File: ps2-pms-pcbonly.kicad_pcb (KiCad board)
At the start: 2 copper layers, 54.7 x 47 mm, 97 parts, among them U1 ADP151, U2 SC174, U3 TPS61253, U4 BQ24076, U5 CSD22202W15

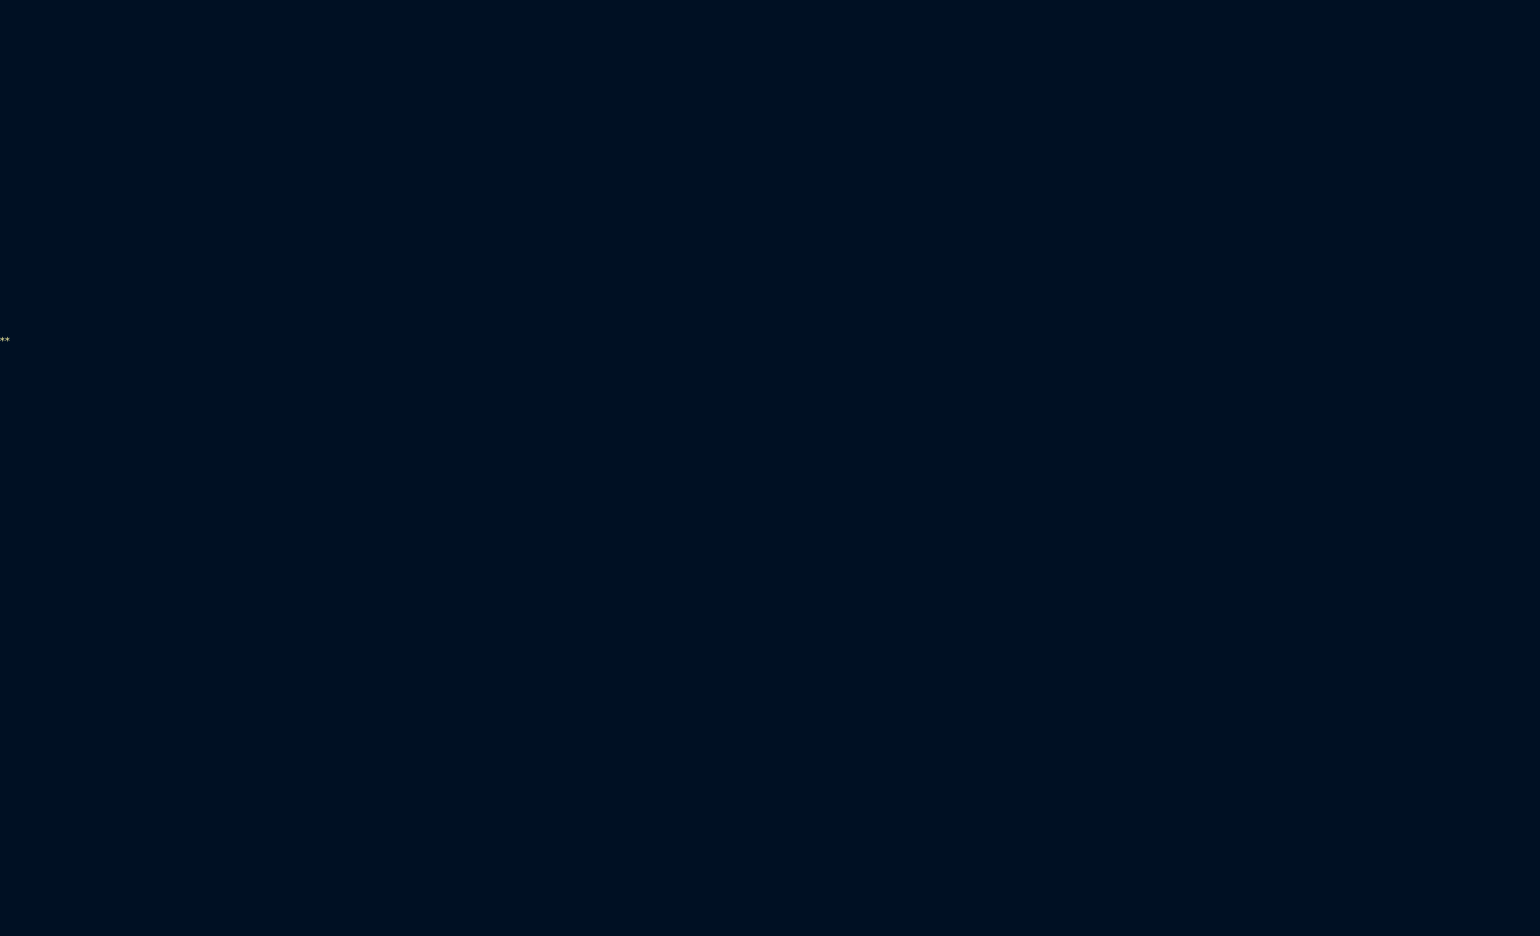
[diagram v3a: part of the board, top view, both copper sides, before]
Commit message: build(ps2-pms): New version with less dead space, shrunk PCB down by 2x1cm
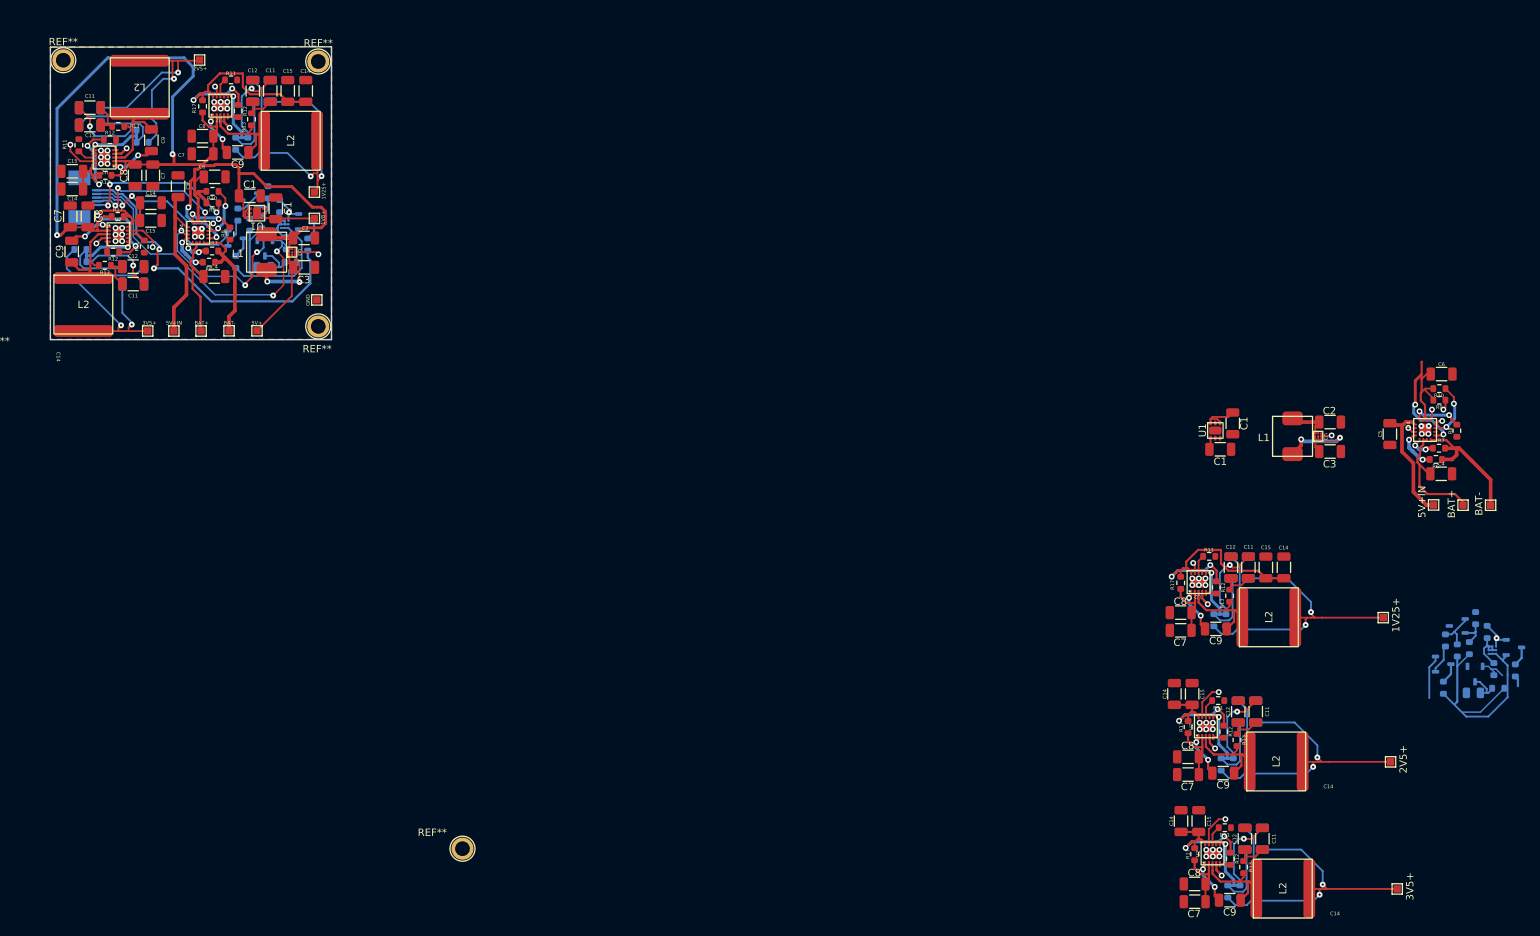
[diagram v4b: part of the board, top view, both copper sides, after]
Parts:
- added 1V25+: TestPoint_Pad_1.0x1.0mm, TestPoint:TestPoint_Pad_1.0x1.0mm, F.Cu at (261.5, 92.8)
- added 1V25+: TestPoint_Pad_1.0x1.0mm, TestPoint:TestPoint_Pad_1.0x1.0mm, F.Cu at (116.3, 35.0)
- added 1V8+: TestPoint_Pad_1.0x1.0mm, TestPoint:TestPoint_Pad_1.0x1.0mm, F.Cu at (116.3, 38.5)
- added 2V5+: TestPoint_Pad_1.0x1.0mm, TestPoint:TestPoint_Pad_1.0x1.0mm, F.Cu at (100.7, 17.0)
- added 2V5+: TestPoint_Pad_1.0x1.0mm, TestPoint:TestPoint_Pad_1.0x1.0mm, F.Cu at (262.5, 112.4)
- added 3V5+: TestPoint_Pad_1.0x1.0mm, TestPoint:TestPoint_Pad_1.0x1.0mm, F.Cu at (93.6, 53.9)
- added 3V5+: TestPoint_Pad_1.0x1.0mm, TestPoint:TestPoint_Pad_1.0x1.0mm, F.Cu at (263.4, 129.7)
- added 5-pin: 5pin FPC, ps2+:5pin FPC, B.Cu at (83.3, 35.7)
- added 5V+: TestPoint_Pad_1.0x1.0mm, TestPoint:TestPoint_Pad_1.0x1.0mm, F.Cu at (108.5, 53.8)
- added 5V+IN: TestPoint_Pad_1.0x1.0mm, TestPoint:TestPoint_Pad_1.0x1.0mm, F.Cu at (97.2, 53.9)
- added 5V+IN: TestPoint_Pad_1.0x1.0mm, TestPoint:TestPoint_Pad_1.0x1.0mm, F.Cu at (268.4, 77.5)
- added BAT+: TestPoint_Pad_1.0x1.0mm, TestPoint:TestPoint_Pad_1.0x1.0mm, F.Cu at (272.4, 77.5)
- added BAT+: TestPoint_Pad_1.0x1.0mm, TestPoint:TestPoint_Pad_1.0x1.0mm, F.Cu at (100.9, 53.9)
- added BAT-: TestPoint_Pad_1.0x1.0mm, TestPoint:TestPoint_Pad_1.0x1.0mm, F.Cu at (104.7, 53.8)
- added BAT-: TestPoint_Pad_1.0x1.0mm, TestPoint:TestPoint_Pad_1.0x1.0mm, F.Cu at (276.1, 77.5)
- added BC846: BC846A, ps2-pms:BC846A, B.Cu at (274.0, 100.5)
- added BC846: BC846A, ps2-pms:BC846A, B.Cu at (279.3, 96.8)
- added BC846: BC846A, ps2-pms:BC846A, B.Cu at (109.5, 42.6)
- added BC846: BC846A, ps2-pms:BC846A, B.Cu at (115.2, 39.0)
- added BC847C: BC846A, ps2-pms:BC846A, B.Cu at (269.7, 99.1)
- added BC847C: BC846A, ps2-pms:BC846A, B.Cu at (105.6, 41.2)
- added C1: C_1206_3216Metric, Capacitor_SMD:C_1206_3216Metric, F.Cu at (239.4, 69.9)
- added C1: 1uF, Capacitor_SMD:C_1206_3216Metric, F.Cu at (107.5, 35.5)
- added C1: C_1206_3216Metric, Capacitor_SMD:C_1206_3216Metric, F.Cu at (111.0, 37.2)
- added C1: 1uF, Capacitor_SMD:C_1206_3216Metric, F.Cu at (241.1, 66.4)
- added C10: C_1206_3216Metric, Capacitor_SMD:C_1206_3216Metric, B.Cu at (107.9, 21.2)
- added C10: C_1206_3216Metric, Capacitor_SMD:C_1206_3216Metric, B.Cu at (240.8, 86.0)
- added C10: C_1206_3216Metric, Capacitor_SMD:C_1206_3216Metric, B.Cu at (91.7, 45.1)
- added C10: C_1206_3216Metric, Capacitor_SMD:C_1206_3216Metric, B.Cu at (85.8, 25.9)
- added C10: C_1206_3216Metric, Capacitor_SMD:C_1206_3216Metric, B.Cu at (241.8, 105.6)
- added C10: C_1206_3216Metric, Capacitor_SMD:C_1206_3216Metric, B.Cu at (242.7, 122.8)
- added C11: C_1206_3216Metric, Capacitor_SMD:C_1206_3216Metric, F.Cu at (85.8, 23.5)
- added C11: C_1206_3216Metric, Capacitor_SMD:C_1206_3216Metric, F.Cu at (243.2, 86.0)
- added C11: C_1206_3216Metric, Capacitor_SMD:C_1206_3216Metric, F.Cu at (245.1, 122.8)
- added C11: C_1206_3216Metric, Capacitor_SMD:C_1206_3216Metric, F.Cu at (110.3, 21.2)
- added C11: C_1206_3216Metric, Capacitor_SMD:C_1206_3216Metric, F.Cu at (91.7, 47.5)
- added C11: C_1206_3216Metric, Capacitor_SMD:C_1206_3216Metric, F.Cu at (244.2, 105.6)
- added C12: C_1206_3216Metric, Capacitor_SMD:C_1206_3216Metric, F.Cu at (240.8, 86.0)
- added C12: C_1206_3216Metric, Capacitor_SMD:C_1206_3216Metric, F.Cu at (241.8, 105.6)
- added C12: C_1206_3216Metric, Capacitor_SMD:C_1206_3216Metric, F.Cu at (91.7, 45.1)
- added C12: C_1206_3216Metric, Capacitor_SMD:C_1206_3216Metric, F.Cu at (242.7, 122.8)
- added C12: C_1206_3216Metric, Capacitor_SMD:C_1206_3216Metric, F.Cu at (85.8, 25.9)
- added C12: C_1206_3216Metric, Capacitor_SMD:C_1206_3216Metric, F.Cu at (107.9, 21.2)
- added C13: C_1206_3216Metric, Capacitor_SMD:C_1206_3216Metric, B.Cu at (91.7, 47.5)
- added C13: C_1206_3216Metric, Capacitor_SMD:C_1206_3216Metric, B.Cu at (110.3, 21.2)
- added C13: C_1206_3216Metric, Capacitor_SMD:C_1206_3216Metric, B.Cu at (85.8, 23.5)
- added C13: C_1206_3216Metric, Capacitor_SMD:C_1206_3216Metric, B.Cu at (245.1, 122.8)
- added C13: C_1206_3216Metric, Capacitor_SMD:C_1206_3216Metric, B.Cu at (243.2, 86.0)
- added C13: C_1206_3216Metric, Capacitor_SMD:C_1206_3216Metric, B.Cu at (244.2, 105.6)
- added C14: C_1206_3216Metric, Capacitor_SMD:C_1206_3216Metric, F.Cu at (115.1, 21.2)
- added C14: C_1206_3216Metric, Capacitor_SMD:C_1206_3216Metric, F.Cu at (94.0, 36.4)
- added C14: C_1206_3216Metric, Capacitor_SMD:C_1206_3216Metric, F.Cu at (248.0, 86.0)
- added C14: C_1206_3216Metric, Capacitor_SMD:C_1206_3216Metric, F.Cu at (234.0, 120.4)
- added C14: C_1206_3216Metric, Capacitor_SMD:C_1206_3216Metric, F.Cu at (233.1, 103.2)
- added C14: C_1206_3216Metric, Capacitor_SMD:C_1206_3216Metric, F.Cu at (83.4, 34.6)
- added C15: C_1206_3216Metric, Capacitor_SMD:C_1206_3216Metric, F.Cu at (235.6, 103.2)
- added C15: C_1206_3216Metric, Capacitor_SMD:C_1206_3216Metric, F.Cu at (236.5, 120.4)
- added C15: C_1206_3216Metric, Capacitor_SMD:C_1206_3216Metric, F.Cu at (112.7, 21.2)
- added C15: C_1206_3216Metric, Capacitor_SMD:C_1206_3216Metric, F.Cu at (94.0, 38.8)
- added C15: C_1206_3216Metric, Capacitor_SMD:C_1206_3216Metric, F.Cu at (83.4, 32.1)
- added C15: C_1206_3216Metric, Capacitor_SMD:C_1206_3216Metric, F.Cu at (245.6, 86.0)
- added C16: C_0805_2012Metric, Capacitor_SMD:C_0805_2012Metric, B.Cu at (109.4, 45.2)
- added C16: C_0805_2012Metric, Capacitor_SMD:C_0805_2012Metric, B.Cu at (273.8, 103.0)
- added C2: C_1206_3216Metric, Capacitor_SMD:C_1206_3216Metric, F.Cu at (254.3, 66.2)
- added C2: C_1206_3216Metric, Capacitor_SMD:C_1206_3216Metric, F.Cu at (114.9, 41.2)
- added C3: C_1206_3216Metric, Capacitor_SMD:C_1206_3216Metric, F.Cu at (114.9, 45.2)
- added C3: C_1206_3216Metric, Capacitor_SMD:C_1206_3216Metric, F.Cu at (254.3, 70.2)
- added C4: C_1206_3216Metric, Capacitor_SMD:C_1206_3216Metric, F.Cu at (102.7, 46.5)
- added C4: C_1206_3216Metric, Capacitor_SMD:C_1206_3216Metric, F.Cu at (269.4, 73.3)
- added C5: C_1206_3216Metric, Capacitor_SMD:C_1206_3216Metric, F.Cu at (97.8, 34.2)
- added C5: C_1206_3216Metric, Capacitor_SMD:C_1206_3216Metric, F.Cu at (262.4, 67.9)
- added C6: C_1206_3216Metric, Capacitor_SMD:C_1206_3216Metric, F.Cu at (102.7, 32.9)
- added C6: C_1206_3216Metric, Capacitor_SMD:C_1206_3216Metric, F.Cu at (269.5, 59.7)
- added C7: C_1206_3216Metric, Capacitor_SMD:C_1206_3216Metric, F.Cu at (235.9, 131.4)
- added C7: C_1206_3216Metric, Capacitor_SMD:C_1206_3216Metric, F.Cu at (234.0, 94.5)
- added C7: C_1206_3216Metric, Capacitor_SMD:C_1206_3216Metric, F.Cu at (101.1, 29.8)
- added C7: C_1206_3216Metric, Capacitor_SMD:C_1206_3216Metric, F.Cu at (83.1, 38.3)
- added C7: C_1206_3216Metric, Capacitor_SMD:C_1206_3216Metric, F.Cu at (94.3, 32.7)
- added C7: C_1206_3216Metric, Capacitor_SMD:C_1206_3216Metric, F.Cu at (235.0, 114.1)
- added C8: C_1206_3216Metric, Capacitor_SMD:C_1206_3216Metric, F.Cu at (235.0, 111.7)
- added C8: C_1206_3216Metric, Capacitor_SMD:C_1206_3216Metric, F.Cu at (234.0, 92.1)
- added C8: C_1206_3216Metric, Capacitor_SMD:C_1206_3216Metric, F.Cu at (101.1, 27.4)
- added C8: C_1206_3216Metric, Capacitor_SMD:C_1206_3216Metric, F.Cu at (235.9, 129.0)
- added C8: C_1206_3216Metric, Capacitor_SMD:C_1206_3216Metric, F.Cu at (91.9, 32.7)
- added C8: C_1206_3216Metric, Capacitor_SMD:C_1206_3216Metric, F.Cu at (85.5, 38.3)
- added C9: C_1206_3216Metric, Capacitor_SMD:C_1206_3216Metric, F.Cu at (83.3, 43.1)
- added C9: C_1206_3216Metric, Capacitor_SMD:C_1206_3216Metric, F.Cu at (238.8, 94.3)
- added C9: C_1206_3216Metric, Capacitor_SMD:C_1206_3216Metric, F.Cu at (240.7, 131.2)
- added C9: C_1206_3216Metric, Capacitor_SMD:C_1206_3216Metric, F.Cu at (94.1, 27.9)
- added C9: C_1206_3216Metric, Capacitor_SMD:C_1206_3216Metric, F.Cu at (239.8, 113.9)
- added C9: C_1206_3216Metric, Capacitor_SMD:C_1206_3216Metric, F.Cu at (105.9, 29.6)
- added G***: LOGO, graphics:iblis 5mm, B.Cu at (90.3, 38.2)
- added GND: TestPoint_Pad_1.0x1.0mm, TestPoint:TestPoint_Pad_1.0x1.0mm, F.Cu at (116.6, 49.6)
- added L1: Inductor-1uH, ps2-pms:Inductor-1uH, F.Cu at (109.8, 43.1)
- added L1: Inductor-1uH, ps2-pms:Inductor-1uH, F.Cu at (249.2, 68.2)
- added L2: inductor-2uh, ps2-pms:inductor-2uh, F.Cu at (113.0, 28.0)
- added L2: inductor-2uh, ps2-pms:inductor-2uh, F.Cu at (92.5, 20.7)
- added L2: inductor-2uh, ps2-pms:inductor-2uh, F.Cu at (247.9, 129.6)
- added L2: inductor-2uh, ps2-pms:inductor-2uh, F.Cu at (246.0, 92.8)
- added L2: inductor-2uh, ps2-pms:inductor-2uh, F.Cu at (84.9, 50.2)
- added L2: inductor-2uh, ps2-pms:inductor-2uh, F.Cu at (247.0, 112.3)
- added R1: R_0603_1608Metric, Resistor_SMD:R_0603_1608Metric, B.Cu at (110.0, 35.0)
- added R1: R_0603_1608Metric, Resistor_SMD:R_0603_1608Metric, B.Cu at (274.1, 92.9)
- added R10: R_0603_1608Metric, Resistor_SMD:R_0603_1608Metric, F.Cu at (102.4, 34.9)
- added R10: R_0603_1608Metric, Resistor_SMD:R_0603_1608Metric, F.Cu at (269.2, 61.7)
- added R11: R_0603_1608Metric, Resistor_SMD:R_0603_1608Metric, F.Cu at (239.1, 104.1)
- added R11: R_0603_1608Metric, Resistor_SMD:R_0603_1608Metric, F.Cu at (105.0, 19.7)
- added R11: R_0603_1608Metric, Resistor_SMD:R_0603_1608Metric, F.Cu at (237.9, 84.5)
- added R11: R_0603_1608Metric, Resistor_SMD:R_0603_1608Metric, F.Cu at (84.3, 28.6)
- added R11: R_0603_1608Metric, Resistor_SMD:R_0603_1608Metric, F.Cu at (240.0, 121.3)
- added R11: R_0603_1608Metric, Resistor_SMD:R_0603_1608Metric, F.Cu at (93.2, 42.4)
- added R12: R_0603_1608Metric, Resistor_SMD:R_0603_1608Metric, F.Cu at (239.8, 108.3)
- added R12: R_0603_1608Metric, Resistor_SMD:R_0603_1608Metric, F.Cu at (105.9, 23.9)
- added R12: R_0603_1608Metric, Resistor_SMD:R_0603_1608Metric, F.Cu at (88.9, 43.1)
- added R12: R_0603_1608Metric, Resistor_SMD:R_0603_1608Metric, F.Cu at (238.8, 88.7)
- added R12: R_0603_1608Metric, Resistor_SMD:R_0603_1608Metric, F.Cu at (240.8, 125.6)
- added R12: R_0603_1608Metric, Resistor_SMD:R_0603_1608Metric, F.Cu at (88.5, 27.9)
- added R13: R_0603_1608Metric, Resistor_SMD:R_0603_1608Metric, F.Cu at (242.6, 126.7)
- added R13: R_0603_1608Metric, Resistor_SMD:R_0603_1608Metric, F.Cu at (89.6, 26.1)
- added R13: R_0603_1608Metric, Resistor_SMD:R_0603_1608Metric, F.Cu at (240.7, 89.8)
- added R13: R_0603_1608Metric, Resistor_SMD:R_0603_1608Metric, F.Cu at (241.7, 109.4)
- added R13: R_0603_1608Metric, Resistor_SMD:R_0603_1608Metric, F.Cu at (107.7, 25.1)
- added R13: R_0603_1608Metric, Resistor_SMD:R_0603_1608Metric, F.Cu at (87.8, 44.9)
- added R14: R_0603_1608Metric, Resistor_SMD:R_0603_1608Metric, B.Cu at (105.6, 28.4)
- added R14: R_0603_1608Metric, Resistor_SMD:R_0603_1608Metric, B.Cu at (238.5, 93.2)
- added R15: R_0603_1608Metric, Resistor_SMD:R_0603_1608Metric, B.Cu at (240.2, 93.2)
- added R15: R_0603_1608Metric, Resistor_SMD:R_0603_1608Metric, B.Cu at (107.2, 28.4)
- added R15: R_0603_1608Metric, Resistor_SMD:R_0603_1608Metric, B.Cu at (241.2, 112.7)
- added R15: R_0603_1608Metric, Resistor_SMD:R_0603_1608Metric, B.Cu at (92.9, 26.6)
- added R15: R_0603_1608Metric, Resistor_SMD:R_0603_1608Metric, B.Cu at (84.5, 44.4)
- added R15: R_0603_1608Metric, Resistor_SMD:R_0603_1608Metric, B.Cu at (242.1, 130.0)
- added R17: R_0603_1608Metric, Resistor_SMD:R_0603_1608Metric, F.Cu at (101.1, 23.3)
- added R17: R_0603_1608Metric, Resistor_SMD:R_0603_1608Metric, B.Cu at (275.7, 94.7)
- added R17: R_0603_1608Metric, Resistor_SMD:R_0603_1608Metric, B.Cu at (111.5, 36.9)
- added R17: R_0603_1608Metric, Resistor_SMD:R_0603_1608Metric, F.Cu at (234.0, 88.1)
- added R17: R_0603_1608Metric, Resistor_SMD:R_0603_1608Metric, F.Cu at (235.9, 124.9)
- added R17: R_0603_1608Metric, Resistor_SMD:R_0603_1608Metric, F.Cu at (89.5, 38.3)
- added R17: R_0603_1608Metric, Resistor_SMD:R_0603_1608Metric, F.Cu at (87.9, 32.7)
- added R17: R_0603_1608Metric, Resistor_SMD:R_0603_1608Metric, F.Cu at (235.0, 107.7)
- added R18: R_0603_1608Metric, Resistor_SMD:R_0603_1608Metric, B.Cu at (279.5, 100.0)
- added R18: R_0603_1608Metric, Resistor_SMD:R_0603_1608Metric, B.Cu at (115.4, 42.1)
- added R19: R_0603_1608Metric, Resistor_SMD:R_0603_1608Metric, B.Cu at (276.6, 99.8)
- added R19: R_0603_1608Metric, Resistor_SMD:R_0603_1608Metric, B.Cu at (112.5, 41.9)
- added R2: R_0603_1608Metric, Resistor_SMD:R_0603_1608Metric, B.Cu at (109.1, 39.1)
- added R2: R_0603_1608Metric, Resistor_SMD:R_0603_1608Metric, B.Cu at (273.2, 96.9)
- added R20: R_0603_1608Metric, Resistor_SMD:R_0603_1608Metric, B.Cu at (113.0, 44.5)
- added R20: R_0603_1608Metric, Resistor_SMD:R_0603_1608Metric, B.Cu at (277.2, 102.4)
- added R21: R_0603_1608Metric, Resistor_SMD:R_0603_1608Metric, B.Cu at (239.5, 112.7)
- added R21: R_0603_1608Metric, Resistor_SMD:R_0603_1608Metric, B.Cu at (92.9, 28.2)
- added R22: R_0603_1608Metric, Resistor_SMD:R_0603_1608Metric, B.Cu at (240.4, 130.0)
- added R22: R_0603_1608Metric, Resistor_SMD:R_0603_1608Metric, B.Cu at (84.5, 42.8)
- added R3: R_0603_1608Metric, Resistor_SMD:R_0603_1608Metric, B.Cu at (270.0, 95.9)
- added R3: R_0603_1608Metric, Resistor_SMD:R_0603_1608Metric, B.Cu at (105.9, 38.0)
- added R4: R_0603_1608Metric, Resistor_SMD:R_0603_1608Metric, B.Cu at (107.5, 39.4)
- added R4: R_0603_1608Metric, Resistor_SMD:R_0603_1608Metric, B.Cu at (271.6, 97.3)
- added R5: R_0603_1608Metric, Resistor_SMD:R_0603_1608Metric, B.Cu at (269.7, 102.3)
- added R5: R_0603_1608Metric, Resistor_SMD:R_0603_1608Metric, B.Cu at (105.6, 44.5)
- added R6: R_0603_1608Metric, Resistor_SMD:R_0603_1608Metric, F.Cu at (268.7, 71.3)
- added R6: R_0603_1608Metric, Resistor_SMD:R_0603_1608Metric, F.Cu at (102.0, 44.5)
- added R7: R_0603_1608Metric, Resistor_SMD:R_0603_1608Metric, F.Cu at (269.1, 69.8)
- added R7: R_0603_1608Metric, Resistor_SMD:R_0603_1608Metric, F.Cu at (102.4, 43.0)
- added R8: R_0603_1608Metric, Resistor_SMD:R_0603_1608Metric, F.Cu at (104.8, 40.6)
- added R8: R_0603_1608Metric, Resistor_SMD:R_0603_1608Metric, F.Cu at (271.5, 67.4)
- added R9: R_0603_1608Metric, Resistor_SMD:R_0603_1608Metric, F.Cu at (269.2, 63.3)
- added R9: R_0603_1608Metric, Resistor_SMD:R_0603_1608Metric, F.Cu at (102.4, 36.5)
- added REF**: TestPoint_Plated_Hole_D2.0mm, TestPoint:TestPoint_Plated_Hole_D2.0mm, F.Cu at (116.8, 53.2)
- added REF**: TestPoint_Plated_Hole_D2.0mm, TestPoint:TestPoint_Plated_Hole_D2.0mm, F.Cu at (116.8, 17.2)
- added REF**: TestPoint_Plated_Hole_D2.0mm, TestPoint:TestPoint_Plated_Hole_D2.0mm, F.Cu at (82.2, 17.1)
- added REF**: TestPoint_Plated_Hole_D2.0mm, TestPoint:TestPoint_Plated_Hole_D2.0mm, F.Cu at (136.4, 124.2)
- added TL431: TL431, ps2-pms:TL431, B.Cu at (271.6, 93.9)
- added TL431: TL431, ps2-pms:TL431, B.Cu at (107.5, 36.1)
- added U1: ADP151, ps2-pms:ADP151, F.Cu at (238.7, 67.4)
- added U1: ADP151, ps2-pms:ADP151, F.Cu at (108.5, 37.8)
- added U2: SC174, ps2-pms:SC174, F.Cu at (238.3, 124.8)
- added U2: SC174, ps2-pms:SC174, F.Cu at (103.5, 23.2)
- added U2: SC174, ps2-pms:SC174, F.Cu at (236.4, 88.0)
- added U2: SC174, ps2-pms:SC174, F.Cu at (89.7, 40.7)
- added U2: SC174, ps2-pms:SC174, F.Cu at (87.8, 30.3)
- added U2: SC174, ps2-pms:SC174, F.Cu at (237.4, 107.6)
- added U3: TPS61253, ps2-pms:TPS61253, F.Cu at (252.7, 68.2)
- added U3: TPS61253, ps2-pms:TPS61253, F.Cu at (113.3, 43.1)
- added U4: BQ24076, ps2-pms:BQ24076, F.Cu at (100.5, 40.5)
- added U4: BQ24076, ps2-pms:BQ24076, F.Cu at (267.2, 67.3)
- added U5: CSD22202W15, ucb-c adapter:CSD22202W15, B.Cu at (112.2, 39.4)
- added U5: CSD22202W15, ucb-c adapter:CSD22202W15, B.Cu at (276.4, 97.2)
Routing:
- net 3V8+: track 154.7 -> 379.7 mm, vias 6 -> 12
- net FB: track 93.1 -> 260.4 mm, vias 6 -> 18
- net VDD: track 59.1 -> 192.3 mm, vias 6 -> 18
- net LX: track 89.1 -> 205.0 mm, vias 2 -> 6
- net 1v25+: track 32.0 -> 128.9 mm, vias 2 -> 6
- net BAT+: track 107.4 -> 203.5 mm
- net 2V5+: track 33.1 -> 128.8 mm, vias 2 -> 6
- net 3V5+: track 43.6 -> 133.3 mm, vias 2 -> 6
- net BTN+: track 48.1 -> 95.9 mm, vias 1 -> 3
- net BTN-: track 47.9 -> 95.4 mm, vias 1 -> 3
- net SYSOFF: track 41.0 -> 81.2 mm, vias 1 -> 5
- net GND: track 17.3 -> 56.3 mm, vias 39 -> 99
- net 5V+IN: track 20.8 -> 59.8 mm
- net BAT-: track 20.2 -> 56.9 mm
- net BST: track 20.4 -> 56.0 mm, vias 6 -> 18
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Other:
- board size 54.7 x 47 mm -> 105.7 x 47 mm
- board text added: "C14"
- board text added: "U5"

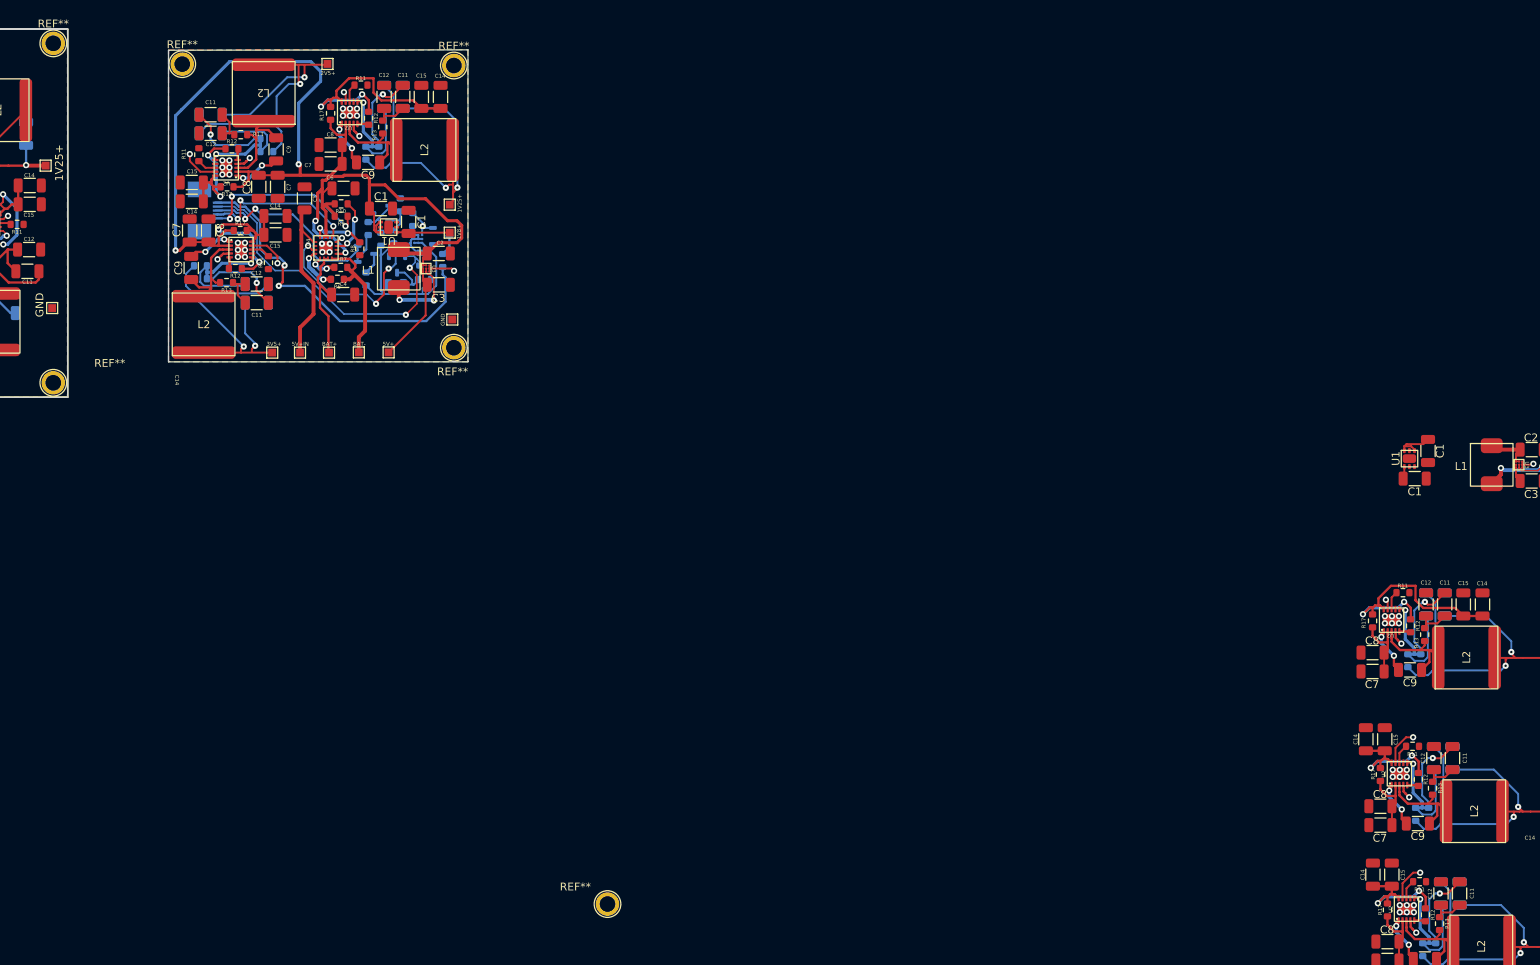
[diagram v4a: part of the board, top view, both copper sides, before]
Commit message: build(pms-board): 2.0 build with cleaner contacts, universal ground, and BOM
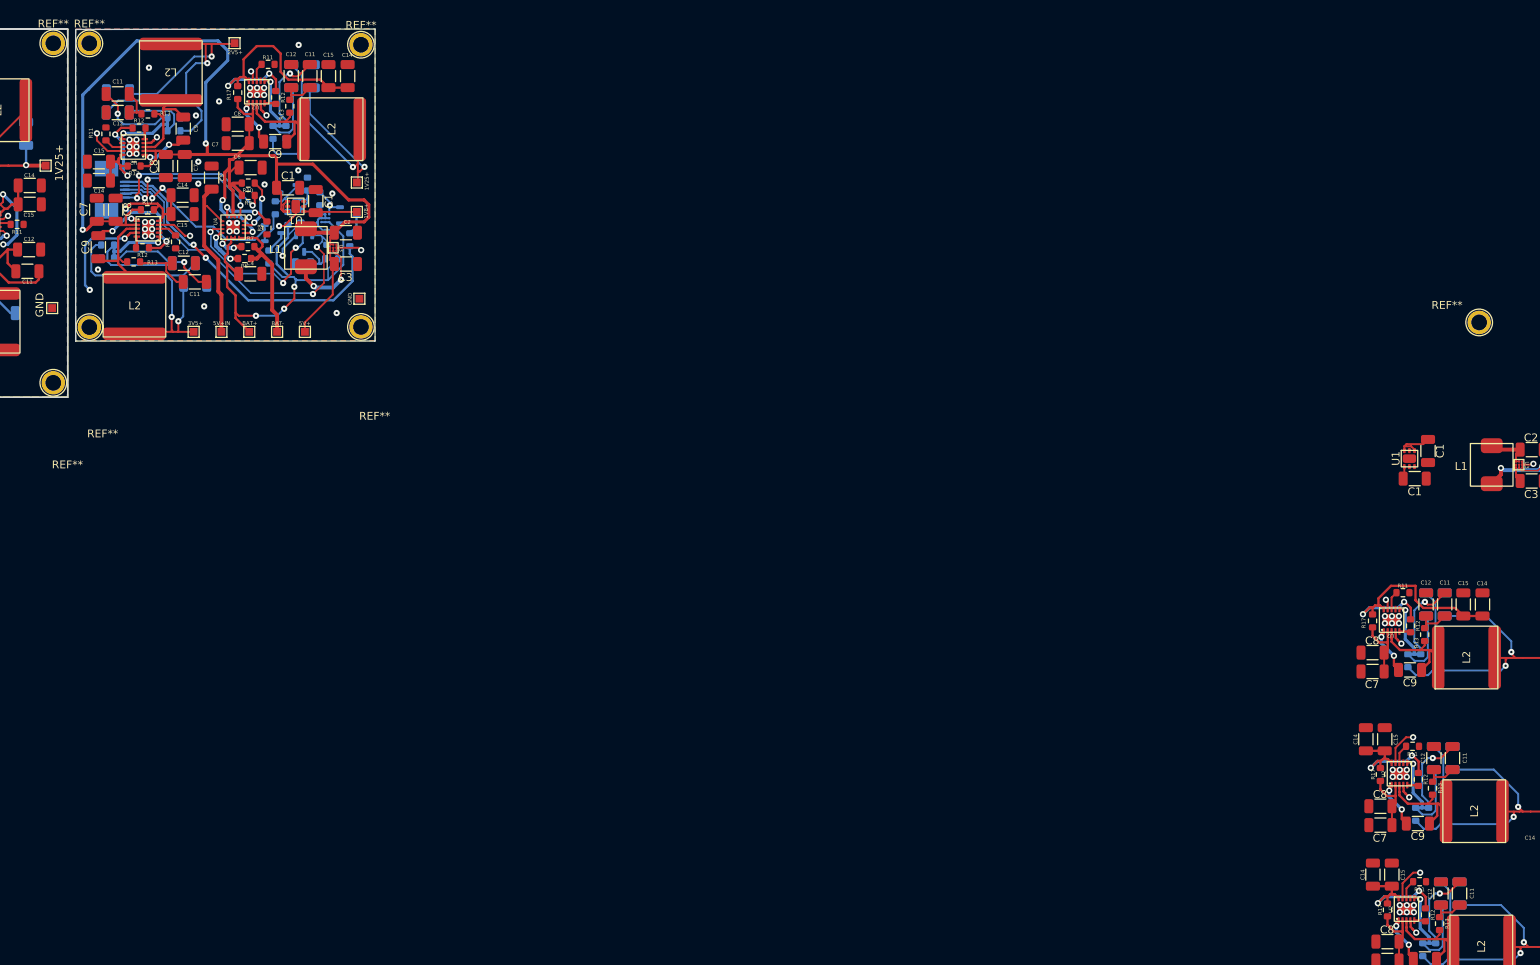
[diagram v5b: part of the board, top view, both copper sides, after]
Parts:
- added REF**: TestPoint_Plated_Hole_D2.0mm, TestPoint:TestPoint_Plated_Hole_D2.0mm, F.Cu at (70.3, 50.6)
- moved REF** 133.7 mm to (247.6, 50.0)
- moved G*** 18.0 mm to (75.9, 49.0)
- moved R5 12.7 mm to (93.2, 41.6)
- moved C13 12.2 mm to (74.0, 20.5)
- moved 1V25+ 12.2 mm to (104.4, 32.1)
- moved 1V8+ 12.1 mm to (104.4, 35.9)
- moved 5-pin 12.1 mm to (71.4, 33.1)
- moved BC847C 12.1 mm to (93.7, 38.6)
- moved C1 12.1 mm to (99.2, 34.5)
- moved C10 12.1 mm to (96.0, 18.6)
- moved C11 12.1 mm to (98.4, 18.6)
- moved C12 12.1 mm to (96.0, 18.6)
- moved C15 12.1 mm to (100.8, 18.6)
- moved C16 12.1 mm to (97.5, 42.5)
- moved C7 12.1 mm to (89.2, 27.1)
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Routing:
- net GND: track 56.3 -> 74.5 mm, vias 99 -> 114
- net BAT+: track 203.5 -> 219.2 mm, vias 1 -> 4
- net FB: track 260.4 -> 266.3 mm
- net LX: track 205.0 -> 209.1 mm
- net BTN+: track 95.9 -> 92.7 mm
- net 2V5+: track 128.8 -> 131.4 mm
- net VDD: track 192.3 -> 194.7 mm
- net RLED: track 40.9 -> 39.8 mm
- net 3V5+: track 133.3 -> 132.4 mm
- net SW: track 35.2 -> 36.0 mm
- net 5V+IN: track 59.8 -> 60.4 mm
- net 1v25+: track 128.9 -> 129.5 mm
- net SYSOFF: track 81.2 -> 80.6 mm
- net Cathode: track 62.1 -> 62.7 mm
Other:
- board size 105.7 x 47 mm -> 93.9 x 47 mm

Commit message: build(final-push): final push
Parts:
- moved R12 1.87 mm to (58.0, 41.4)
- moved U1 1.87 mm to (97.9, 36.6)
- moved U2 1.87 mm to (79.0, 39.5)
- moved 1V25+ 1.87 mm to (66.0, 31.4)
- moved C10 1.87 mm to (97.3, 20.0)
- moved C11 1.87 mm to (99.7, 20.0)
- moved C12 1.87 mm to (97.3, 20.0)
- moved C14 1.87 mm to (104.5, 20.0)
- moved C15 1.87 mm to (102.0, 20.0)
- moved C7 1.87 mm to (90.5, 28.5)
- moved C8 1.87 mm to (90.5, 26.1)
- moved C9 1.87 mm to (83.5, 26.7)
- moved C9 1.87 mm to (95.2, 28.3)
- moved L2 1.87 mm to (81.9, 19.5)
- moved R11 1.87 mm to (94.3, 18.5)
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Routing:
- net 2V5+: track 131.4 -> 133.1 mm
